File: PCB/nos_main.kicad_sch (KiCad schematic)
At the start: 95 parts, among them J1 Conn_01x04, U1 Pico_Trim, U2 ADG732BSUZ

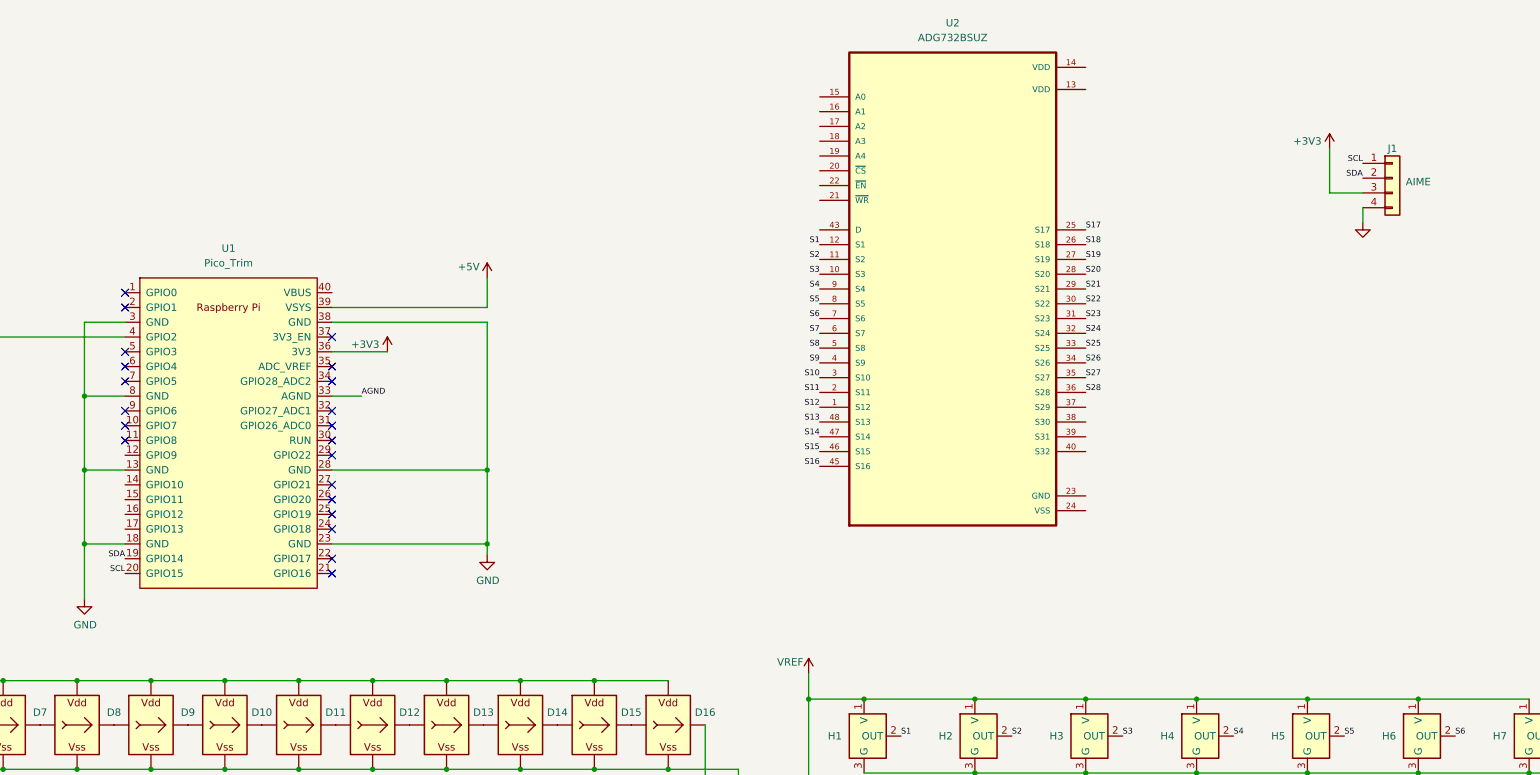
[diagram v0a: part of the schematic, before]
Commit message: Change PCB folder
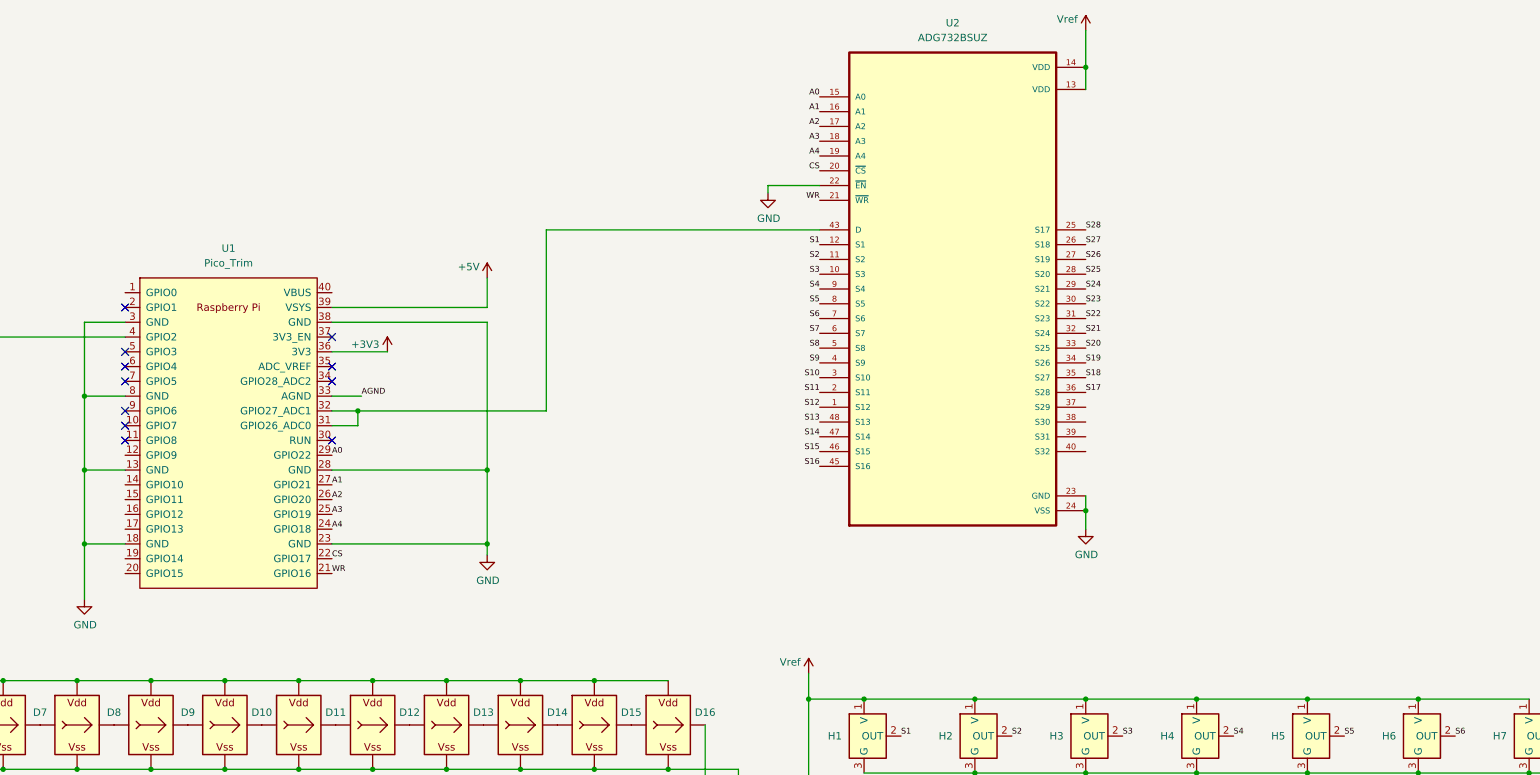
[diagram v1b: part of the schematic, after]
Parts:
- removed J1: Conn_01x04, nos_main:PN532, symbol Connector_Generic:Conn_01x04
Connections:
- net VREF is gone; now on net Vref: H1.1 (V), H10.1 (V), H11.1 (V), H12.1 (V), H13.1 (V), H14.1 (V), H15.1 (V), H16.1 (V), H17.1 (V), H18.1 (V), H19.1 (V), H2.1 (V), H20.1 (V), H21.1 (V), H22.1 (V), H23.1 (V), H24.1 (V), H25.1 (V), H26.1 (V), H27.1 (V), H28.1 (V), H3.1 (V), H4.1 (V), H5.1 (V), H6.1 (V), H7.1 (V), H8.1 (V), H9.1 (V)
- net GND: now also U2.22 (~{EN}), U2.23 (GND), U2.24 (VSS)
- net S17: now also U2.36 (S28); no longer U2.25 (S17)
- net S18: now also U2.35 (S27); no longer U2.26 (S18)
- net S19: now also U2.34 (S26); no longer U2.27 (S19)
- net S20: now also U2.33 (S25); no longer U2.28 (S20)
- net S21: now also U2.32 (S24); no longer U2.29 (S21)
- net S22: now also U2.31 (S23); no longer U2.30 (S22)
- net S23: now also U2.30 (S22); no longer U2.31 (S23)
- net S24: now also U2.29 (S21); no longer U2.32 (S24)
- net S25: now also U2.28 (S20); no longer U2.33 (S25)
- net S26: now also U2.27 (S19); no longer U2.34 (S26)
- net S27: now also U2.26 (S18); no longer U2.35 (S27)
- net S28: now also U2.25 (S17); no longer U2.36 (S28)
- net Vref: now reaches U2.13 (VDD)
- net Vref: now also U2.14 (VDD)
- net A0: now reaches U2.15 (A0)
- net A0: now also U1.29 (GPIO22)
- net A1: now reaches U2.16 (A1)
- net A1: now also U1.27 (GPIO21)
- net A2: now reaches U2.17 (A2)
- net A2: now also U1.26 (GPIO20)
- net A3: now reaches U2.18 (A3)
- net A3: now also U1.25 (GPIO19)
- net A4: now reaches U2.19 (A4)
- net A4: now also U1.24 (GPIO18)
- net CS: now reaches U2.20 (~{CS})
- net CS: now also U1.22 (GPIO17)
- net WR: now reaches U2.21 (~{WR})
- net WR: now also U1.21 (GPIO16)
- net at U2.43 (D): now also U1.31 (GPIO26_ADC0), U1.32 (GPIO27_ADC1)
- net SCL: no longer names the net of U1.20 (GPIO15)
- net SDA: no longer names the net of U1.19 (GPIO14)
- no-connect marks 22 -> 12

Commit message: PCB progress 60%
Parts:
- added U3: DC/DC, nos_main:DCDC_3to5, symbol Connector_Generic:Conn_02x02_Odd_Even
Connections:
- net AGND is gone; now on net GND: H1.3 (G), H10.3 (G), H11.3 (G), H12.3 (G), H13.3 (G), H14.3 (G), H15.3 (G), H16.3 (G), H17.3 (G), H18.3 (G), H19.3 (G), H2.3 (G), H20.3 (G), H21.3 (G), H22.3 (G), H23.3 (G), H24.3 (G), H25.3 (G), H26.3 (G), H27.3 (G), H28.3 (G), H3.3 (G), H4.3 (G), H5.3 (G), H6.3 (G), H7.3 (G), H8.3 (G), H9.3 (G), U1.33 (AGND)
- net +3V3: now also U3.3 (Pin_3)
- net GND: now also U3.1 (Pin_1), U3.2 (Pin_2)
- net Vref: now also U3.4 (Pin_4)
- no-connect marks 12 -> 17

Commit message: PCB progress 80%
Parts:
- added C10, C11, C12, C13, C14, C15, C16, C17, C18, C19, C20, C21, C22, C23, C24, C25, C26, C27, C28, C29, C31, C32, C33, C34, C35, C36, C37, C38, C39, C40, C41, C42, C43, C44, C45, C46, C47, C48, C49, C50, C51, C52, C53, C54, C55, C56, C57, C58, C9: 0.1uF, Capacitor_SMD:C_0603_1608Metric_Pad1.08x0.95mm_HandSolder, symbol Device:C
- added C30: 1nF, Capacitor_SMD:C_0603_1608Metric_Pad1.08x0.95mm_HandSolder, symbol Device:C
- added JP1: SolderJumper_2_Open, Jumper:SolderJumper-2_P1.3mm_Open_RoundedPad1.0x1.5mm, symbol Jumper:SolderJumper_2_Open
- added R1: 2K, Resistor_SMD:R_0603_1608Metric_Pad0.98x0.95mm_HandSolder, symbol Device:R
- added R2: 10K, Resistor_SMD:R_0603_1608Metric_Pad0.98x0.95mm_HandSolder, symbol Device:R
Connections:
- net +3V3: now also JP1.1 (A)
- net +5V: now also C10.1, C11.1, C12.1, C13.1, C14.1, C15.1, C16.1, C17.1, C18.1, C19.1, C20.1, C21.1, C22.1, C23.1, C24.1, C25.1, C26.1, C27.1, C28.1, C9.1
- net GND: now also C10.2, C11.2, C12.2, C13.2, C14.2, C15.2, C16.2, C17.2, C18.2, C19.2, C20.2, C21.2, C22.2, C23.2, C24.2, C25.2, C26.2, C27.2, C28.2, C29.2, C30.2, C31.2, C32.2, C33.2, C34.2, C35.2, C36.2, C37.2, C38.2, C39.2, C40.2, C41.2, C42.2, C43.2, C44.2, C45.2, C46.2, C47.2, C48.2, C49.2, C50.2, C51.2, C52.2, C53.2, C54.2, C55.2, C56.2, C57.2, C58.2, C9.2, R2.1
- net Vref: now also C29.1, C31.1, C32.1, C33.1, C34.1, C35.1, C36.1, C37.1, C38.1, C39.1, C40.1, C41.1, C42.1, C43.1, C44.1, C45.1, C46.1, C47.1, C48.1, C49.1, C50.1, C51.1, C52.1, C53.1, C54.1, C55.1, C56.1, C57.1, C58.1, JP1.2 (B)
- net at U1.31 (GPIO26_ADC0), U1.32 (GPIO27_ADC1): now also C30.1, R1.1, R2.2; no longer U2.43 (D)
- new net: R1.2, U2.43 (D)
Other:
- moved on the sheet: C1, C2, C3, C4, C5, C6, C7, C8, H1, H10, H11, H12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

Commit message: PCB v1.0 done
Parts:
- added C59, C60: 0.1uF, Capacitor_SMD:C_0603_1608Metric_Pad1.08x0.95mm_HandSolder, symbol Device:C
- added D57, D58, D59, D60, D61, D62: WS2812B_Unified, nos_main:WS2812B-4020_UP, symbol nos_main:WS2812B_Unified
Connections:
- net +5V: now also C59.1, C60.1, D57.V (VDD), D58.V (VDD), D59.V (VDD), D60.V (VDD), D61.V (VDD), D62.V (VDD)
- net GND: now also C59.2, C60.2, D57.G (VSS), D58.G (VSS), D59.G (VSS), D60.G (VSS), D61.G (VSS), D62.G (VSS)
- net at U1.1 (GPIO0): now also D57.I (In)
- new net: D58.O (Out), D59.I (In)
- new net: D59.O (Out), D60.I (In)
- new net: D60.O (Out), D61.I (In)
- new net: D57.O (Out), D58.I (In)
- new net: D61.O (Out), D62.I (In)
- no-connect marks 17 -> 16
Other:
- moved on the sheet: C1, C10, C11, C12, C13, C14, C15, C16, C17, C18, C19, C2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

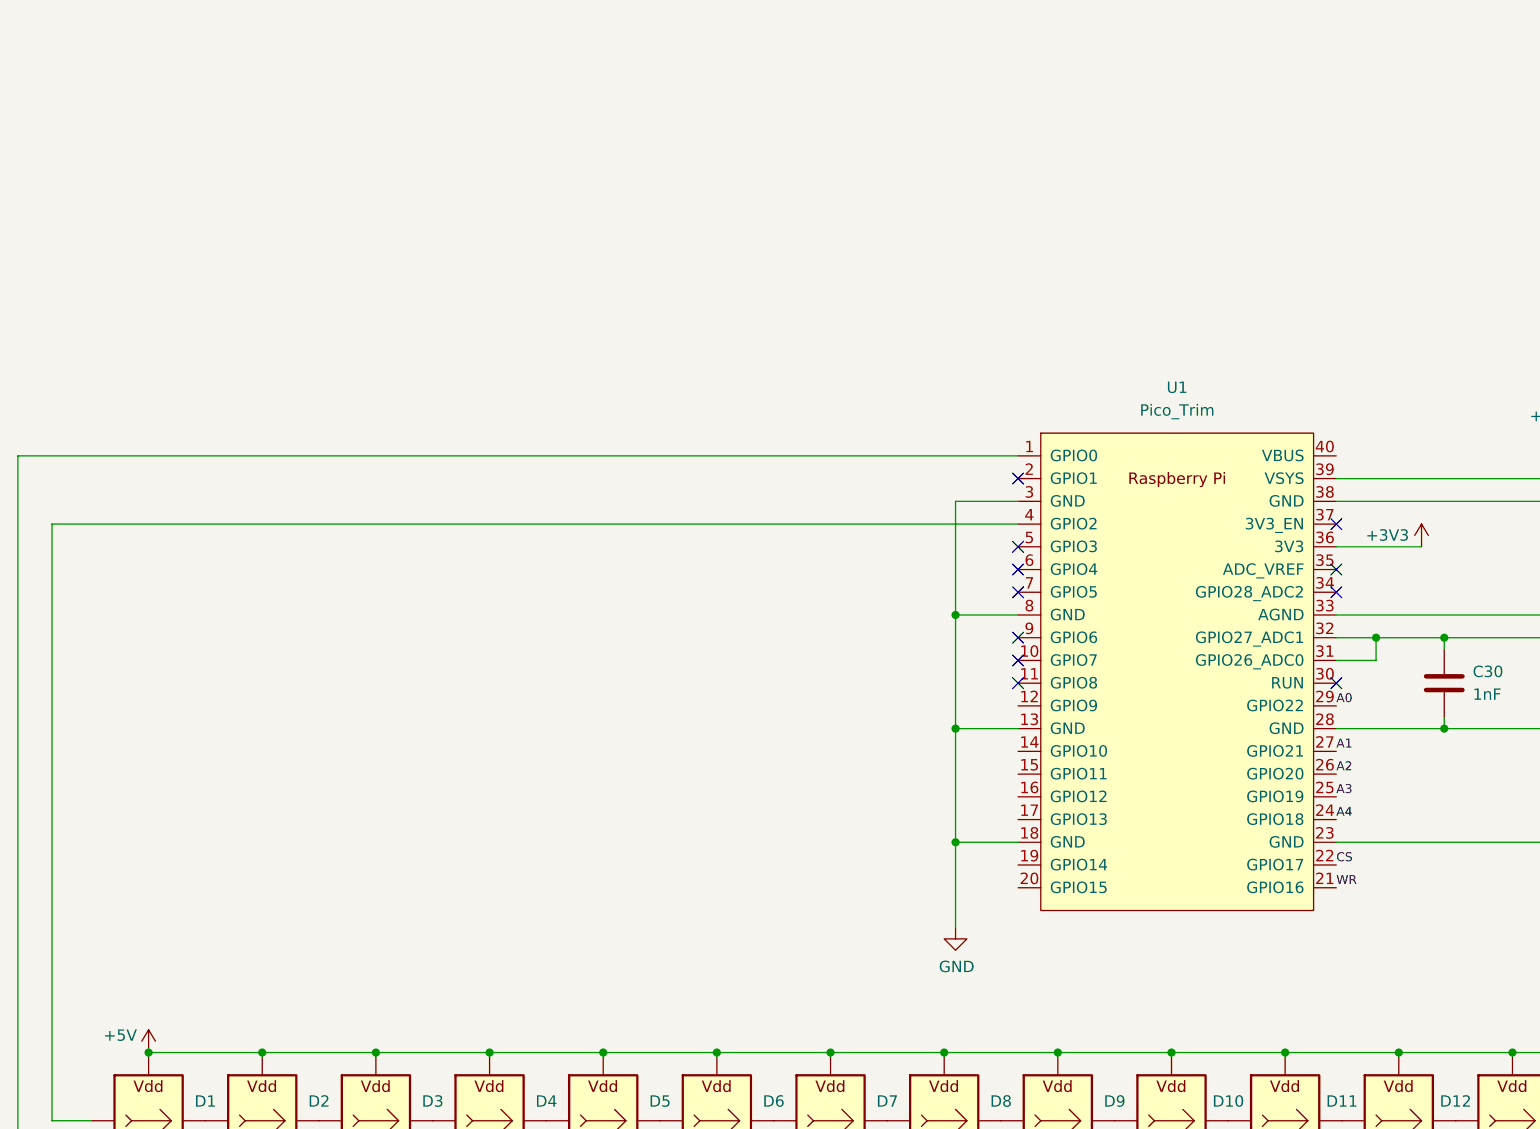
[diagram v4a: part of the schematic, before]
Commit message: PCB v1.1 for dual USB port
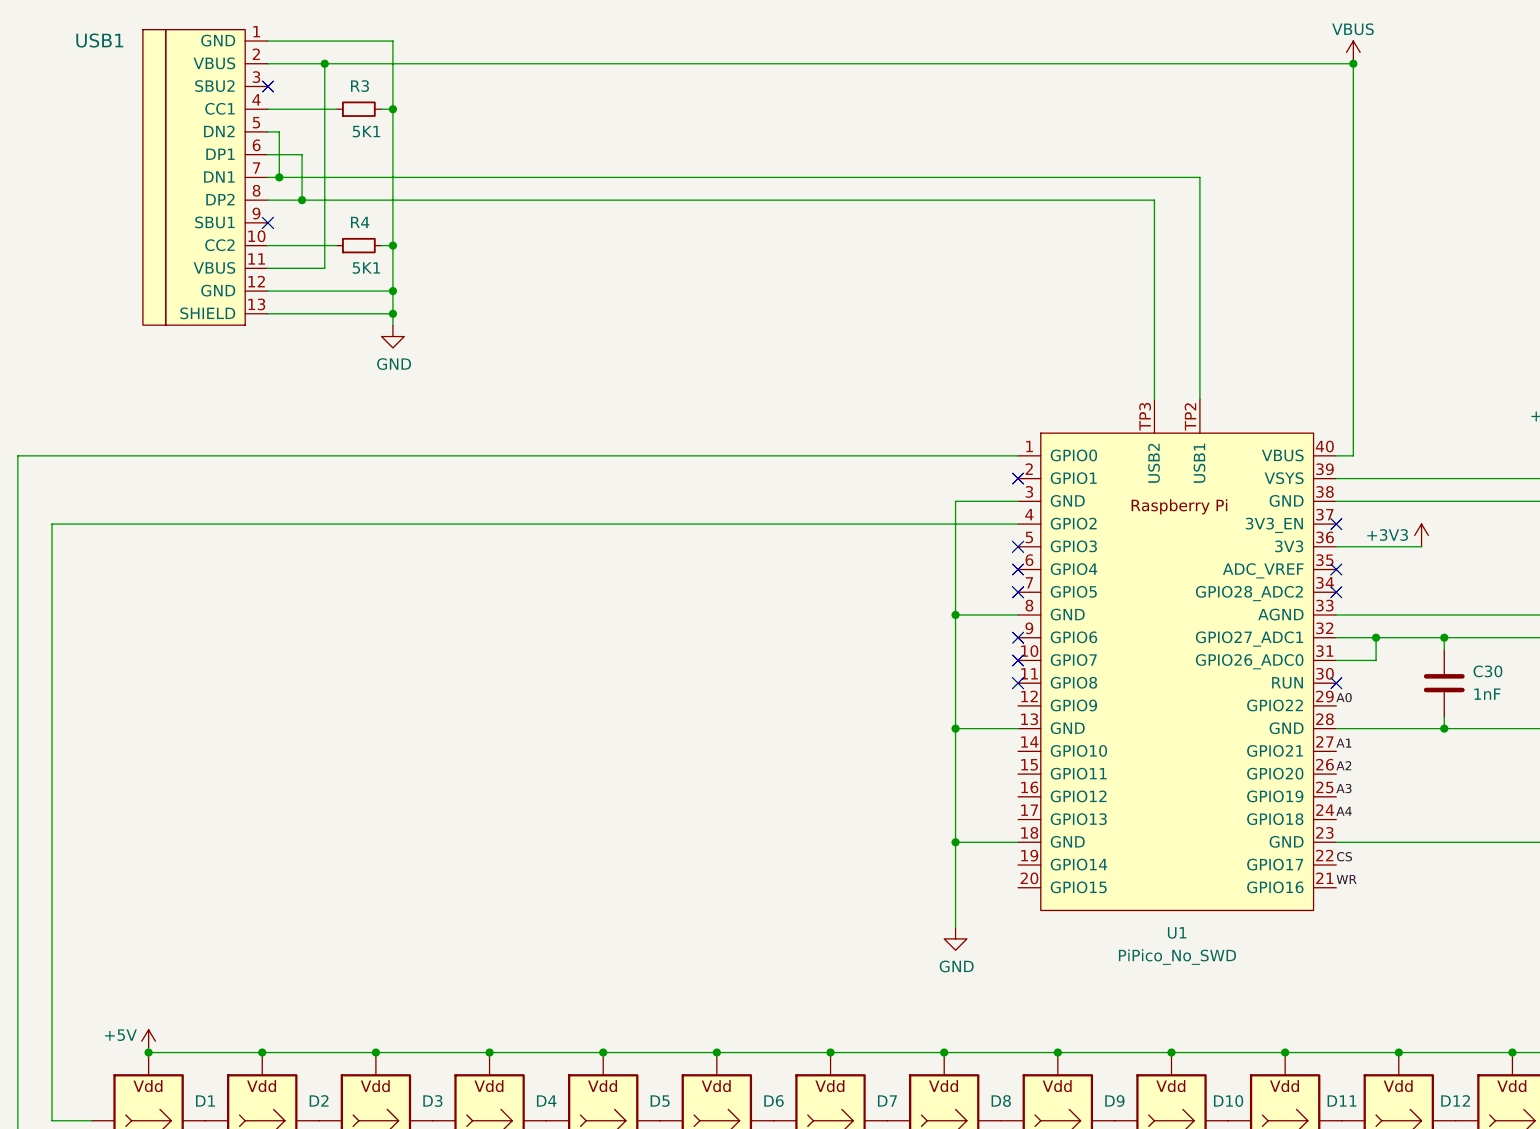
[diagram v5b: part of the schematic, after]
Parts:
- removed U1: Pico_Trim, nos_main:RPi_Pico_SMD_No_USB, symbol nos_main:Pico_Trim
- added R3, R4: 5K1, Resistor_SMD:R_0603_1608Metric_Pad0.98x0.95mm_HandSolder, symbol Device:R_Small
- added U1: PiPico_No_SWD, nos_main:RPi_Pico_SMD_Pins_No_SWD, symbol nos_main:PiPico_No_SWD
- added USB1: U262-161N-4BVC11, Type-C:HRO-TYPE-C-31-M-12-Assembly, symbol Type-C:HRO-TYPE-C-31-M-12
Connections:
- net +3V3: now also U1.36 (3V3)
- net +5V: now also U1.39 (VSYS)
- net A0: now also U1.29 (GPIO22)
- net A1: now also U1.27 (GPIO21)
- net A2: now also U1.26 (GPIO20)
- net A3: now also U1.25 (GPIO19)
- net A4: now also U1.24 (GPIO18)
- net CS: now also U1.22 (GPIO17)
- net GND: now also R3.2, R4.2, U1.13 (GND), U1.18 (GND), U1.23 (GND), U1.28 (GND), U1.3 (GND), U1.33 (AGND), U1.38 (GND), U1.8 (GND), USB1.1 (GND), USB1.12 (GND), USB1.13 (SHIELD)
- net WR: now also U1.21 (GPIO16)
- net at D1.I (In): now also U1.4 (GPIO2)
- net at D57.I (In): now also U1.1 (GPIO0)
- net at C30.1, R1.1, R2.2: now also U1.31 (GPIO26_ADC0), U1.32 (GPIO27_ADC1)
- new net: R4.1, USB1.10 (CC2)
- new net: R3.1, USB1.4 (CC1)
- new net: U1.TP2 (USB1), USB1.5 (DN2), USB1.7 (DN1)
- new net: U1.TP3 (USB2), USB1.6 (DP1), USB1.8 (DP2)
- new net VBUS: U1.40 (VBUS), USB1.11 (VBUS), USB1.2 (VBUS)
- no-connect marks 16 -> 18
